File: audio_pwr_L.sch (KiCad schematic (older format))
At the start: 40 parts, among them Q201 BC546, Q202 BC546, Q203 BC546, Q204 BD140, Q205 BD139, Q206 BD140, Q207 MJL21193, Q208 MJL21194, Q209 BC546

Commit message: Opened on home office computer. Some rescue and lib conversion happened. Need to confirm no changes on work laptop.
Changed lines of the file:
@@
 EESchema Schematic File Version 4
-LIBS:AAMB-cache
 EELAYER 30 0
 EELAYER END
@@
 Connection ~ 7400 3650
 $Comp
-L Power-amp:+35V #PWR?
+L AAMB-rescue:+35V-Power-amp #PWR?
 U 1 1 5E1F9FBF
 P 7925 1850
@@
 	7925 1850 7925 1900
 $Comp
-L Power-amp:-35V #PWR0109
+L AAMB-rescue:-35V-Power-amp #PWR0109
 U 1 1 5E2010CE
 P 8050 5075

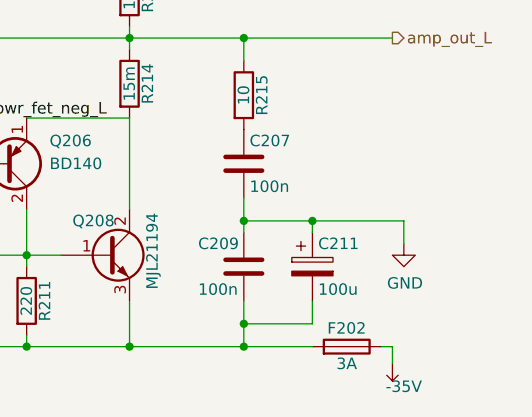
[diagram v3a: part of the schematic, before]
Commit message: Fixed several DRC errors. Tied audoi input returns to GND. Added Switch logic.
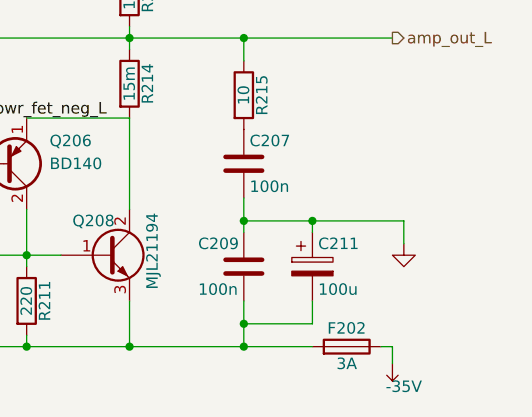
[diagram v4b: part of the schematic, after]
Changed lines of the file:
@@
 EESchema Schematic File Version 4
+LIBS:AAMB-cache
 EELAYER 30 0
 EELAYER END
@@
 pwr_fet_pos_L
 $Comp
-L power:GND #PWR0103
-U 1 1 5E1CCB09
-P 8100 4550
-F 0 "#PWR0103" H 8100 4300 50  0001 C CNN
-F 1 "GND" H 8105 4377 50  0000 C CNN
-F 2 "" H 8100 4550 50  0001 C CNN
-F 3 "" H 8100 4550 50  0001 C CNN
-	1    8100 4550
-	1    0    0    -1
-$EndComp
-$Comp
 L power:GND #PWR0104
 U 1 1 5E1CCB0A
@@
 	5450 3050 5450 3100
 Connection ~ 5450 3050
-Wire Wire Line
-	8100 4550 8100 4450
 Wire Wire Line
 	8100 4450 7700 4450
@@
 Wire Wire Line
 	7300 1900 7450 1900
+$Comp
+L power:GND #PWR0103
+U 1 1 5E35028E
+P 8100 4550
+F 0 "#PWR0103" H 8100 4300 50  0001 C CNN
+F 1 "GND" H 8100 4400 50  0001 C CNN
+F 2 "" H 8100 4550 50  0001 C CNN
+F 3 "" H 8100 4550 50  0001 C CNN
+	1    8100 4550
+	1    0    0    -1
+$EndComp
+Wire Wire Line
+	8100 4550 8100 4450
 $EndSCHEMATC

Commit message: 23JAN2020 daily commit.
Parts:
- R213, R214: footprint Resistor_THT:R_Axial_Power_L25.0mm_W9.0mm_P30.48mm -> Resistor_THT:R_Axial_Power_L25.0mm_W9.0mm_P10.16mm_Vertical
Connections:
- net amp_out_L: now also R214.2; no longer R214.1
- net pwr_fet_neg_L: now also R214.1; no longer R214.2
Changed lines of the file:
@@
 F 0 "R214" V 6980 3850 50  0000 C CNN
 F 1 "15m" V 6900 3850 50  0000 C CNN
-F 2 "Resistor_THT:R_Axial_Power_L25.0mm_W9.0mm_P30.48mm" V 6830 3850 50  0001 C CNN
+F 2 "Resistor_THT:R_Axial_Power_L25.0mm_W9.0mm_P10.16mm_Vertical" V 6830 3850 50  0001 C CNN
 F 3 "" H 6900 3850 50  0001 C CNN
 	1    6900 3850
-	1    0    0    -1
+	-1   0    0    1
 $EndComp
 $Comp
@@
 F 0 "R213" V 6980 3450 50  0000 C CNN
 F 1 "15m" V 6900 3450 50  0000 C CNN
-F 2 "Resistor_THT:R_Axial_Power_L25.0mm_W9.0mm_P30.48mm" V 6830 3450 50  0001 C CNN
+F 2 "Resistor_THT:R_Axial_Power_L25.0mm_W9.0mm_P10.16mm_Vertical" V 6830 3450 50  0001 C CNN
 F 3 "" H 6900 3450 50  0001 C CNN
 	1    6900 3450
@@
 Wire Wire Line
 	8100 4550 8100 4450
+Connection ~ 6900 4000
 $EndSCHEMATC
